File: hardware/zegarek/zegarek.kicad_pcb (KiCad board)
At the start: 2 copper layers, 123.5 x 51 mm, 14 parts, among them J1 Conn_01x02_Socket, J2 Conn_01x02_Pin, Q1 IRF740, U1 MC34063AD

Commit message: Signed-off-by: kwojcik22 <wojcik2k2@gmail.com>
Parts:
- moved J1 1.00 mm to (108.0, 115.0)
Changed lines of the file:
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@@
 	(footprint "Connector:Banana_Jack_2Pin"
 		(layer "F.Cu")
-		(at 109 115 90)
+		(at 108 114.97 90)
 		(descr "Dual banana socket, footprint - 2 x 6mm drills")
 		(tags "banana socket")
@@
 		(tags "resistor handsolder")
 		(property "Reference" "R3"
-			(at 3 0 360)
+			(at 3 0 0)
 			(layer "F.SilkS")
 			(effects
@@
 		)
 		(property "Value" "180"
-			(at 0 1.65 360)
+			(at 0 1.65 0)
 			(layer "F.Fab")
 			(hide yes)
@@
 		)
 		(fp_text user "${REFERENCE}"
-			(at 0 0 360)
+			(at 0 0 0)
 			(layer "F.Fab")
 			(effects
@@
 		)
 		(property "Value" "0R22"
-			(at 0 1.82 360)
+			(at 0 1.82 0)
 			(layer "F.Fab")
 			(hide yes)
@@
 		)
 		(fp_text user "${REFERENCE}"
-			(at 0 0 360)
+			(at 0 0 0)
 			(layer "F.Fab")
 			(effects

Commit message: w3
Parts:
- moved J1 0.73 mm to (108.5, 115.5)
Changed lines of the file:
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@@
 	(footprint "Connector:Banana_Jack_2Pin"
 		(layer "F.Cu")
-		(at 108 114.97 90)
+		(at 108.5 115.5 90)
 		(descr "Dual banana socket, footprint - 2 x 6mm drills")
 		(tags "banana socket")

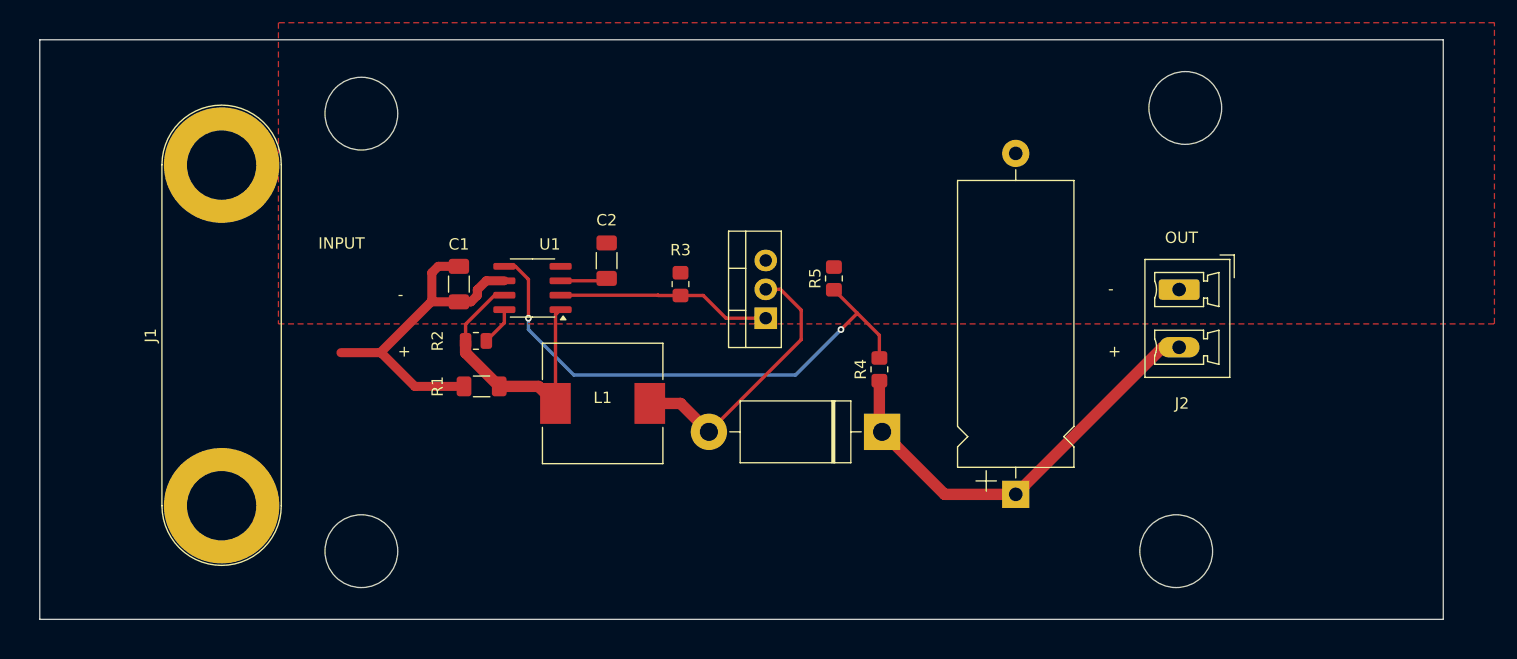
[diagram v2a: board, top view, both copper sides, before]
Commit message: c1 pwr/gnd
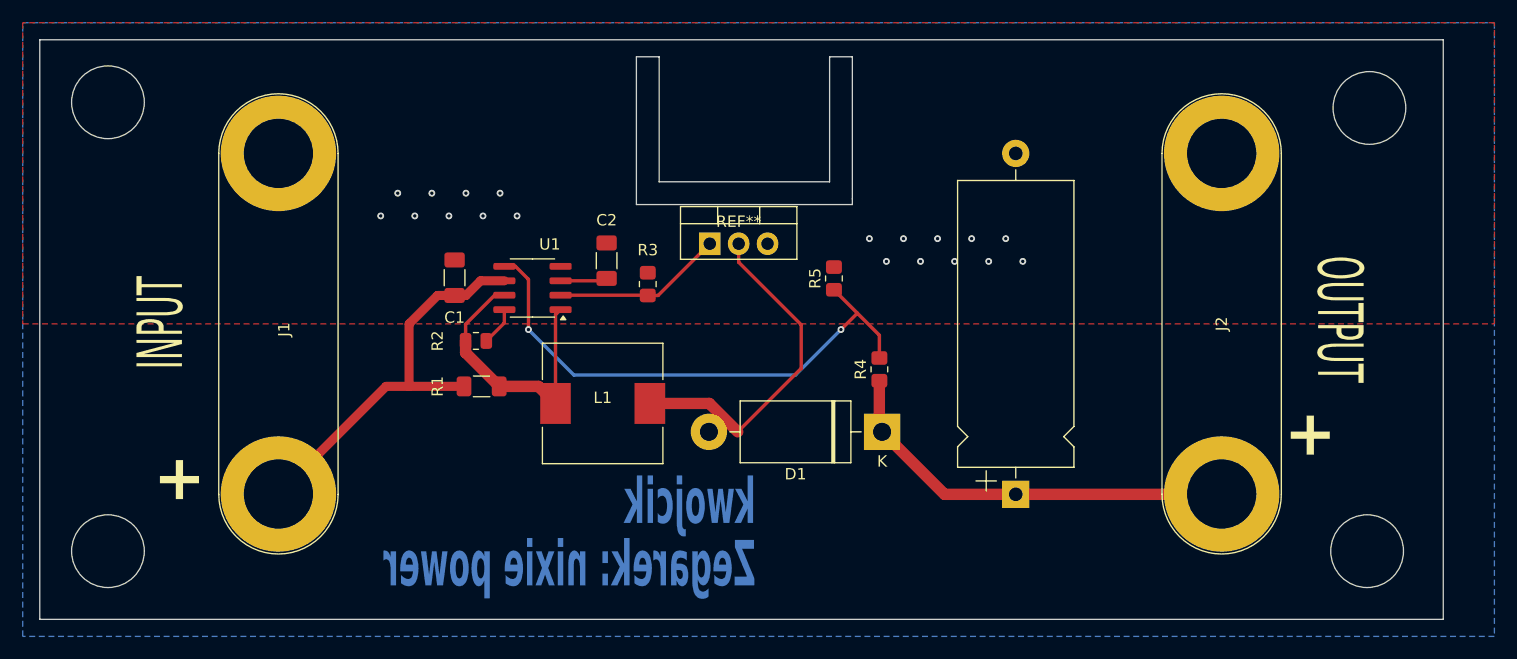
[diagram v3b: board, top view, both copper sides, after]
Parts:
- added REF**: SINK, Heatsink:SINK, F.Cu at (154.0, 91.0)
- J2: footprint Connector_Phoenix_MC_HighVoltage:PhoenixContact_MCV_1,5_2-G-5.08_1x02_P5.08mm_Vertical -> Connector:Banana_Jack_2Pin
- moved J1 31.4 mm to (113.5, 84.5), turned to -90 degrees
- moved J2 12.5 mm to (196.5, 84.5)
- moved Q1 8.20 mm to (151.5, 92.4), turned to 0 degrees
- moved R3 2.88 mm to (146.0, 96.0)
- moved C1 0.68 mm to (129.0, 95.4), turned to -90 degrees
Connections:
- C1 pad 1: +12V -> GND
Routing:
- net Net-(D1-A): track 24.2 -> 29.9 mm
- net +12V: track 31.1 -> 35.7 mm
- net Net-(Q1-G): track 18.9 -> 15.0 mm
- net +VDC: track 38.4 -> 36.8 mm
- net GND: vias 0 -> 19
- added copper zone on B.Cu, net GND
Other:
- outline, holes or cut-outs redrawn
- board text added: "OUTPUT"
- board text added: "Zegarek: nixie power"
- board text added: "kwojcik"
- board text removed: "-"
- board text removed: "OUT"

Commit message: ordered gerber
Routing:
- net Net-(D1-A): track 29.9 -> 25.2 mm
- net Net-(U1-Vfb): track 47.5 -> 44.2 mm
- net Net-(Q1-G): track 15.0 -> 16.5 mm
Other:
- outline, holes or cut-outs redrawn

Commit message: diode correction
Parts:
- D1: value UF5400 -> UF4007
